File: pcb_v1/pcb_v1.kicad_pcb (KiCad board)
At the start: 4 copper layers, 54.2 x 40.5 mm, 10 parts, among them IC1 ESP32-WROOM-32UE-H4, IC2 DWM3000TR13, IC3 TC1017-3.3VLTTR, J1 Conn_02x03_Counter_Clockwise, J2 1769

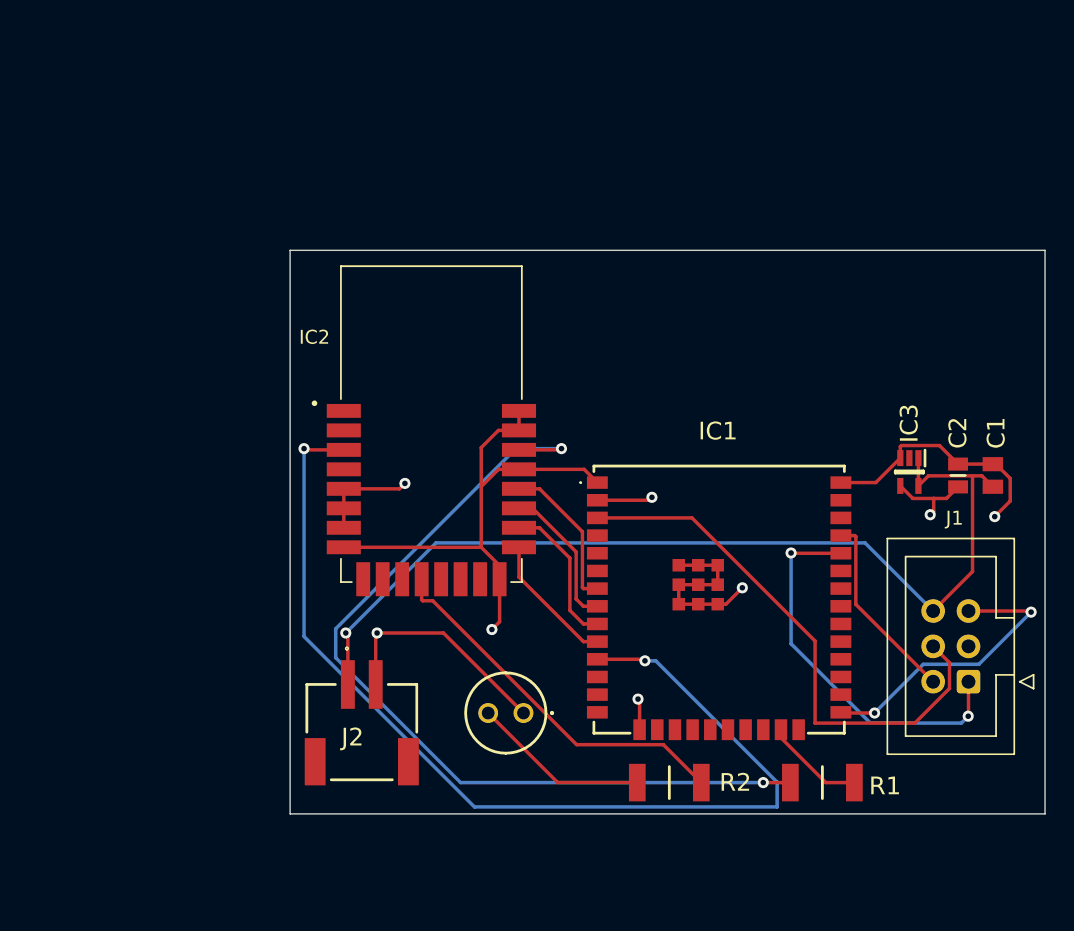
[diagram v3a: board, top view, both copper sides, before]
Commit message: update pcb to use new mcu. the antennas are hanging off the pcb, and there are additional 1x4 pin headers for interfacing with unused GPIO pins just incase, and to flash code rx/tx.
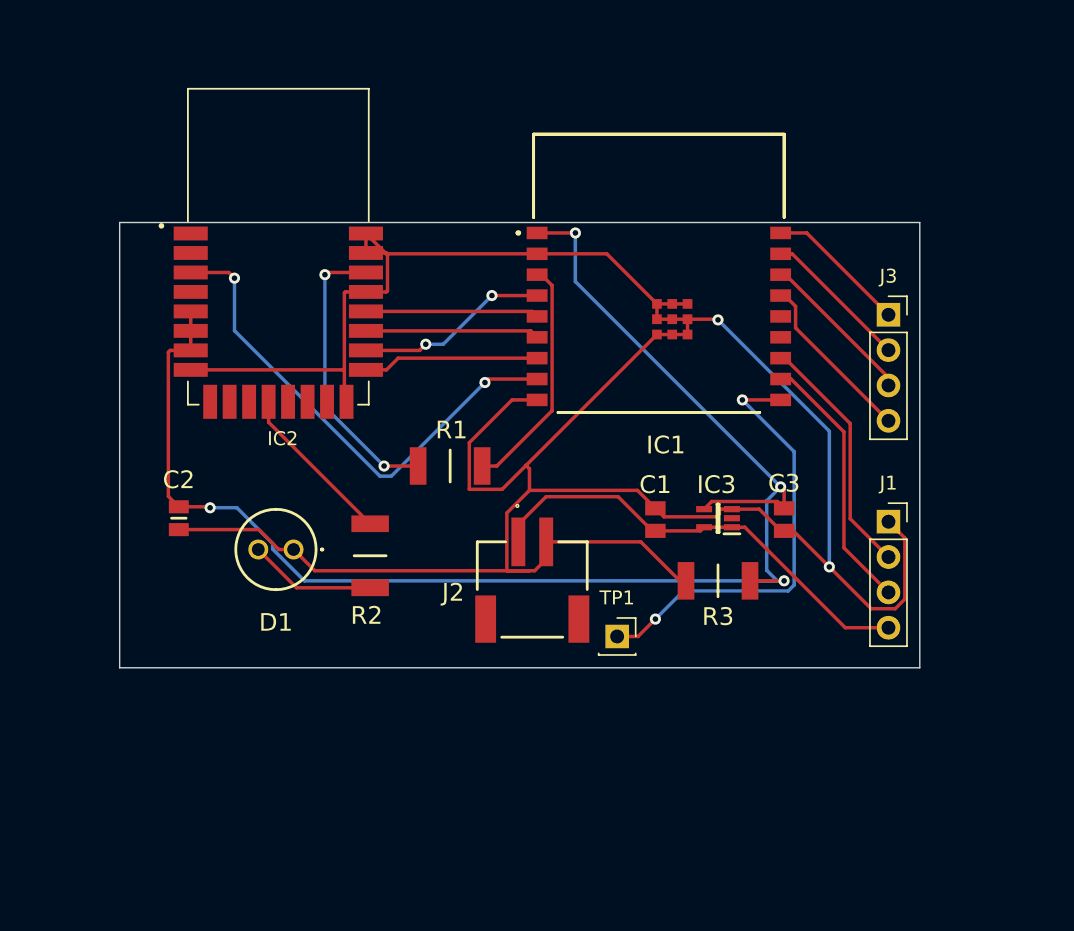
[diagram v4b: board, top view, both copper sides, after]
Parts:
- added C3: 100nF, 100nF_footprint:CAPC2012X94N, F.Cu at (142.2, 106.3)
- added J3: Conn_01x04_Pin, Connector_PinSocket_2.54mm:PinSocket_1x04_P2.54mm_Vertical, F.Cu at (149.8, 91.6)
- added R3: 100k Ohm, 100kOhm_footprint:RESC5025X65N, F.Cu at (137.5, 110.8)
- added TP1: Boot, Connector_PinSocket_2.54mm:PinSocket_1x01_P2.54mm_Vertical, F.Cu at (130.2, 114.8)
- IC1: value ESP32-WROOM-32UE-H4 -> ESP32-C3-WROOM-02-N4; footprint esp32_footprint:ESP32WROOM32UEH4 -> esp_32_c3_footprint:ESP32C3WROOM02N4
- J1: value Conn_02x03_Counter_Clockwise -> Conn_01x04_Pin; footprint Connector_IDC:IDC-Header_2x03_P2.54mm_Vertical -> Connector_PinSocket_2.54mm:PinSocket_1x04_P2.54mm_Vertical
- moved C2 56.1 mm to (98.8, 106.2), turned to -90 degrees
- moved R1 35.1 mm to (118.2, 102.5)
- moved R2 27.0 mm to (112.5, 109.0), turned to -90 degrees
- moved C1 24.5 mm to (133.0, 106.3)
- moved IC1 20.4 mm to (134.2, 92.0)
- moved D1 20.3 mm to (107.0, 108.5)
- moved IC2 16.8 mm to (105.9, 86.7)
- moved J2 16.0 mm to (124.2, 108.0)
- moved IC3 14.1 mm to (137.5, 106.2), turned to 180 degrees
- moved J1 12.9 mm to (149.8, 106.5), turned to 0 degrees
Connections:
- IC1 pad 1: GND -> VDD
- IC1 pad 10: Net-(IC1-IO25) -> Net-(IC1-IO10)
- IC1 pad 11: Net-(IC1-IO26) -> Net-(IC1-RXD)
- IC1 pad 12: unconnected-(IC1-IO27-Pad12) -> Net-(IC1-TXD)
- IC1 pad 15: GND -> Net-(IC1-IO3)
- IC1 pad 16: unconnected-(IC1-IO13-Pad16) -> Net-(IC1-IO2)
- IC1 pad 17: unconnected-(IC1-NC_1-Pad17) -> Net-(IC1-IO1)
- IC1 pad 18: unconnected-(IC1-NC_2-Pad18) -> Net-(IC1-IO0)
- IC1 pad 19: unconnected-(IC1-NC_3-Pad19) -> GND
- IC1 pad 2: VDD -> GND
- IC1 pad 20: unconnected-(IC1-NC_4-Pad20) -> GND
- IC1 pad 21: unconnected-(IC1-NC_5-Pad21) -> GND
- IC1 pad 22: unconnected-(IC1-NC_6-Pad22) -> GND
- IC1 pad 23: Net-(IC1-IO15) -> GND
- IC1 pad 24: unconnected-(IC1-IO2-Pad24) -> GND
- IC1 pad 25: Net-(IC1-IO0) -> GND
- IC1 pad 26: unconnected-(IC1-IO4-Pad26) -> GND
- IC1 pad 27: unconnected-(IC1-IO16-Pad27) -> GND
- IC1 pad 3: Net-(IC1-EN) -> Net-(IC1-IO4)
- IC1 pad 4: unconnected-(IC1-SENSOR_VP-Pad4) -> Net-(IC1-IO5)
- IC1 pad 5: unconnected-(IC1-SENSOR_VN-Pad5) -> Net-(IC1-IO6)
- IC1 pad 6: unconnected-(IC1-IO34-Pad6) -> Net-(IC1-IO7)
- IC1 pad 7: Net-(IC1-IO35) -> Net-(IC1-IO8)
- IC1 pad 8: Net-(IC1-IO32) -> Net-(IC1-IO9)
- IC1 pad 9: Net-(IC1-IO33) -> GND
- IC2 pad 17: Net-(IC1-IO25) -> Net-(IC1-IO8)
- IC2 pad 18: Net-(IC1-IO33) -> Net-(IC1-IO5)
- IC2 pad 19: Net-(IC1-IO32) -> Net-(IC1-IO7)
- IC2 pad 20: Net-(IC1-IO35) -> Net-(IC1-IO6)
- IC2 pad 3: Net-(IC1-IO26) -> Net-(IC1-IO9)
- J1 pad 1: Net-(IC1-RXD0) -> GND
- J1 pad 2: Net-(IC1-TXD0) -> Net-(IC1-TXD)
- J1 pad 3: GND -> Net-(IC1-RXD)
- J1 pad 4: Net-(IC1-EN) -> Net-(IC3-VIN)
- R1 pad 2: Net-(IC1-IO15) -> Net-(IC1-IO4)
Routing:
- net Net-(IC1-IO26): track 73.8 -> 0.00 mm, vias 2 -> 0
- net VDD: track 56.2 -> 107.2 mm, vias 3 -> 4
- net Net-(IC2-GPIO8): track 63.1 -> 21.0 mm
- net GND: track 157.1 -> 198.3 mm, vias 5 -> 2
- net Net-(IC1-EN): track 39.4 -> 0.00 mm
- net Net-(IC3-VIN): track 69.5 -> 32.8 mm, vias 1 -> 0
- net Net-(IC1-IO9): track 0.00 -> 36.1 mm, vias 0 -> 2
- net Net-(IC1-IO10): track 0.00 -> 31.9 mm, vias 0 -> 2
- net Net-(IC1-RXD0): track 27.9 -> 0.00 mm, vias 2 -> 0
- net Net-(IC1-RXD): track 0.00 -> 19.0 mm
- net Net-(IC1-TXD): track 0.00 -> 17.7 mm
- net Net-(IC1-IO4): track 0.00 -> 17.1 mm
- net Net-(IC2-GPIO3): track 27.0 -> 11.8 mm
- net Net-(IC1-IO5): track 0.00 -> 13.9 mm, vias 0 -> 2
- net Net-(IC1-TXD0): track 13.8 -> 0.00 mm
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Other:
- board size 54.2 x 40.5 mm -> 57.5 x 32 mm
- copper layers 4 -> 2
- board text removed: "SDP TEAM 8 SWAN v1"
